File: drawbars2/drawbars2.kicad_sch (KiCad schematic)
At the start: 20 parts, among them J1 Conn_01x08, U1 4051, U2 4051

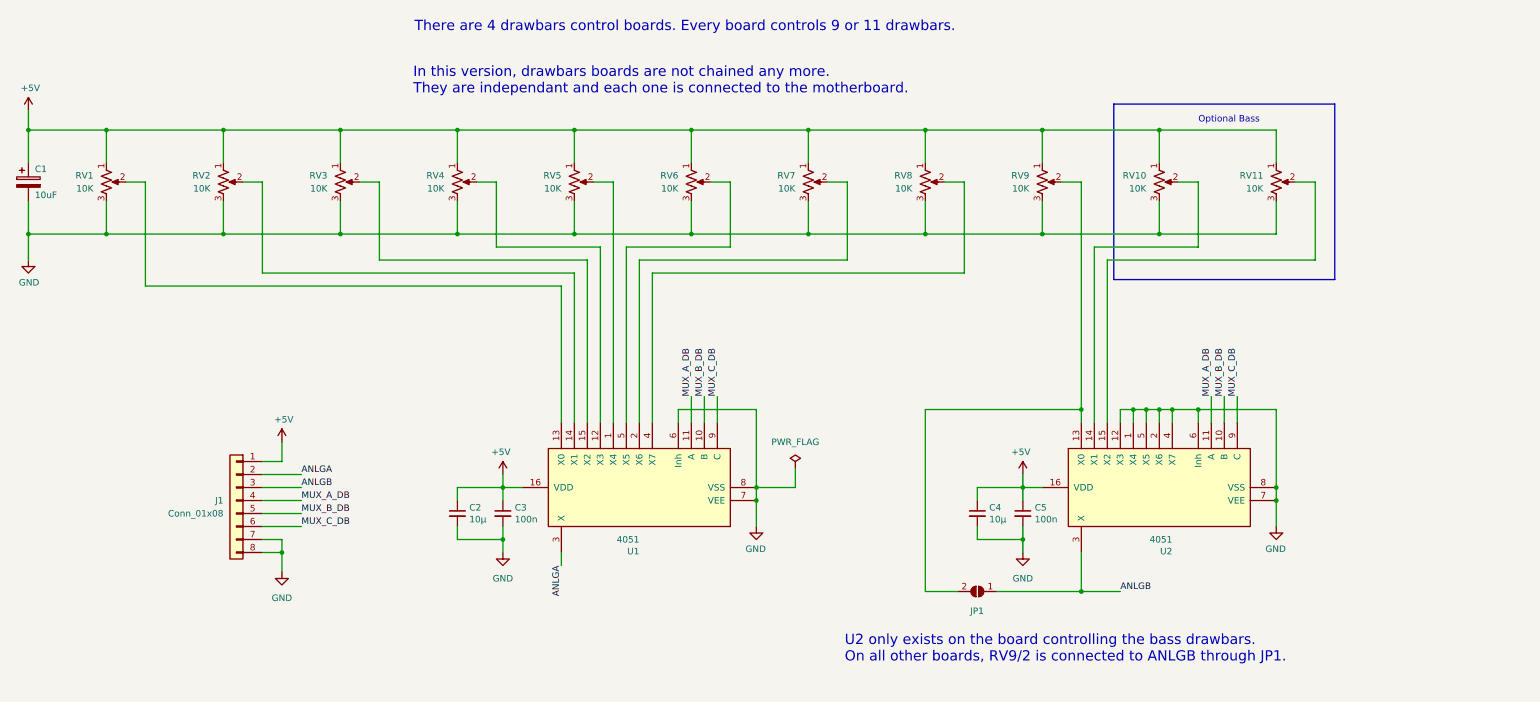
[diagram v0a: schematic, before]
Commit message: New organ architecture with mother board
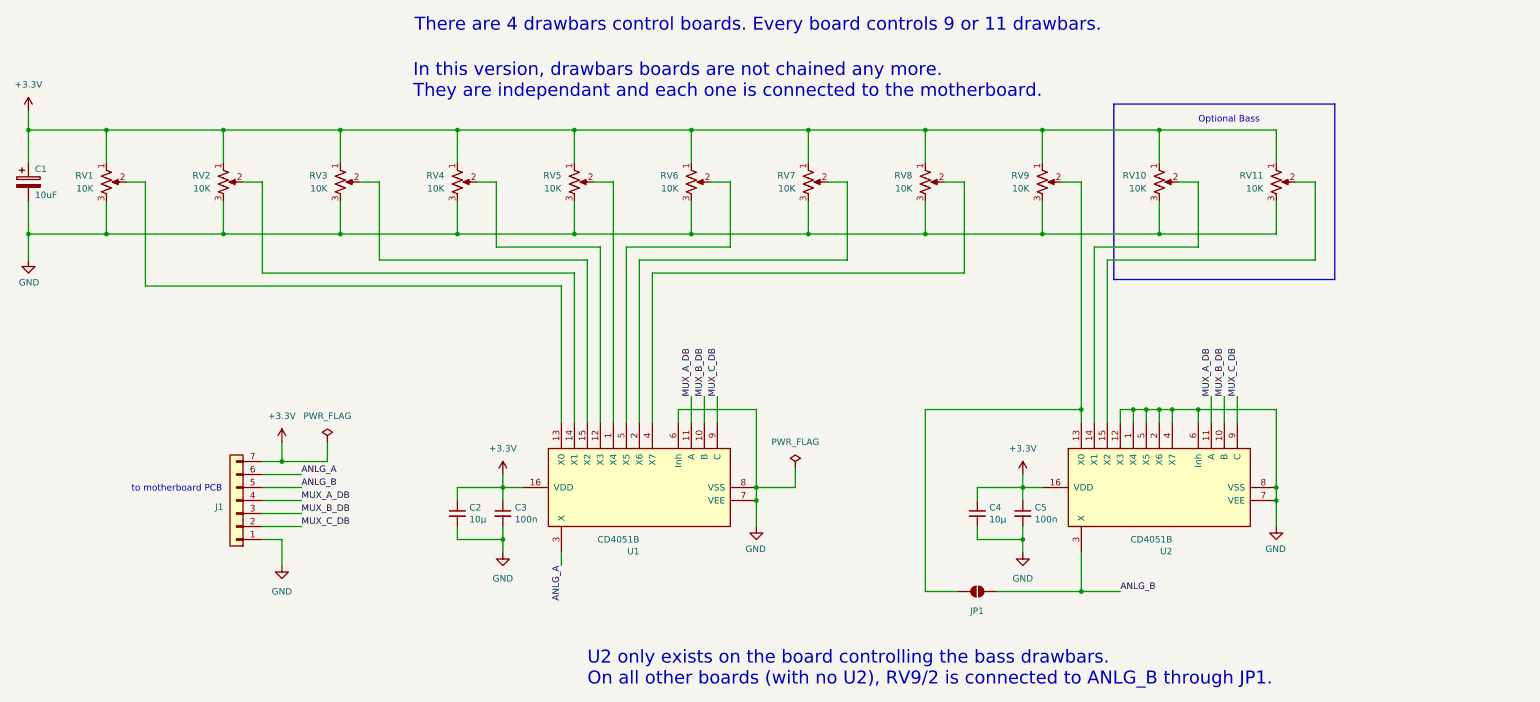
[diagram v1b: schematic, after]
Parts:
- removed J1: Conn_01x08, symbol Connector_Generic:Conn_01x08
- added J1: Conn_01x07, symbol Connector_Generic:Conn_01x07
- U1, U2: value 4051 -> CD4051B
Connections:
- net GND: now also J1.1 (Pin_1)
- net MUX_A_DB: now also J1.4 (Pin_4)
- net MUX_B_DB: now also J1.3 (Pin_3)
- net MUX_C_DB: now also J1.2 (Pin_2)
- net +5V renamed +3.3V
- net +3.3V: now also J1.7 (Pin_7)
- net ANLGA renamed ANLG_A
- net ANLG_A: now also J1.6 (Pin_6)
- net ANLGB renamed ANLG_B
- net ANLG_B: now also J1.5 (Pin_5)
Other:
- note added: "U2 only exists on the board controlling the bass drawbars. On all other boards (with no U2), RV9/2 is connected to ANLG_B through JP1."
- note added: "to motherboard PCB"
- note removed: "U2 only exists on the board controlling the bass drawbars. On all other boards, RV9/2 is connected to ANLGB through JP1."
